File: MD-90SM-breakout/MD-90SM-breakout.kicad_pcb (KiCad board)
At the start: 2 copper layers, 21 x 14.6 mm, 13 parts, among them CON1 MD-90SM

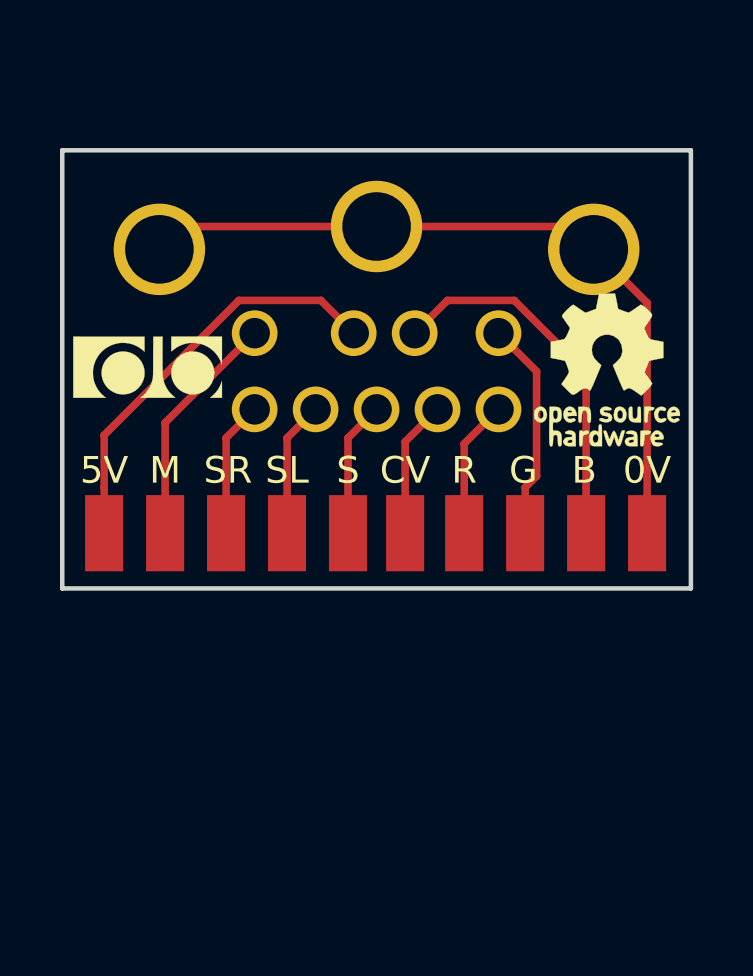
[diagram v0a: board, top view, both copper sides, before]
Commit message: updated to v0.2 with breadboard compatible dip spacing
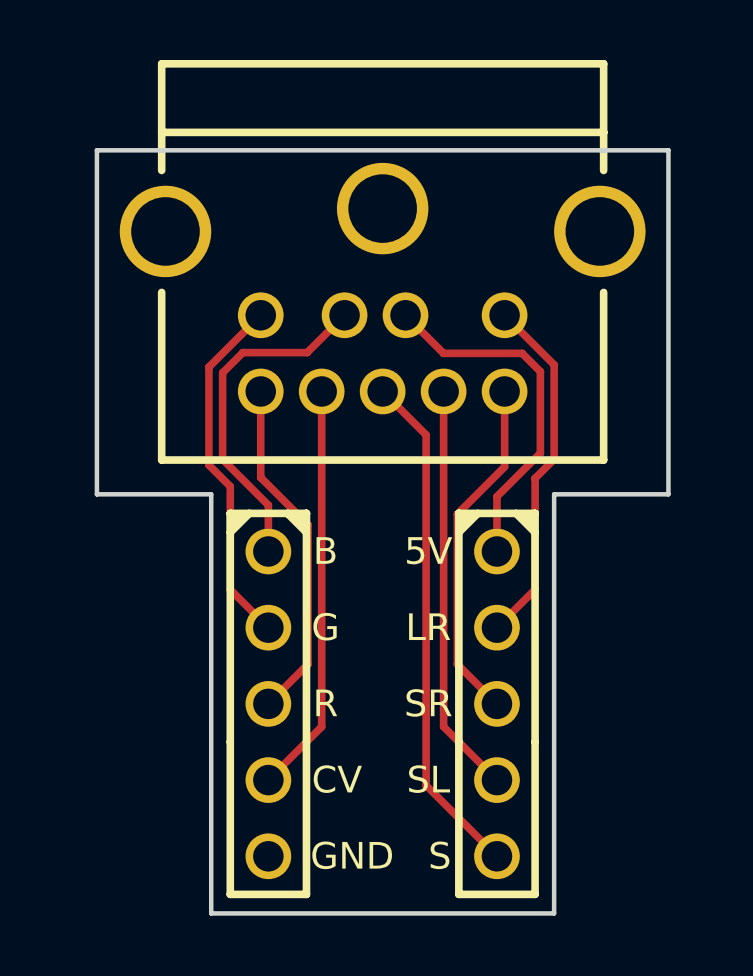
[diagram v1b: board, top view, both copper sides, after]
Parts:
- removed CON1: MD-90SM, db-thparts:MD-90SM
- removed G***: LOGO, db-artwork:db-logo_5mm
- removed G***: LOGO, db-artwork:oshw-logo_5mm
- removed TP1, TP10, TP2, TP3, TP4, TP5, TP6, TP7, TP8, TP9: TP_50x100, db-smt:TP_50-100
- added CON101: MD-90SM, db-thparts:MD-90SM, F.Cu at (149.7, 95.7)
- added CON102: PH1-05-UA, db-thparts:HDR1X5, F.Cu at (145.9, 101.0)
- added CON103: PH1-05-UA, db-thparts:HDR1X5, F.Cu at (153.6, 101.0)
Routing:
- net /GND: track 25.3 -> 0.00 mm
- net (no net): track 18.8 -> 0.00 mm
- net /S: track 4.52 -> 17.1 mm
- net /SL: track 4.52 -> 13.7 mm
- net /CV: track 4.57 -> 13.7 mm
- net /SR: track 4.52 -> 11.6 mm
- net /R: track 4.60 -> 11.6 mm
- net /G: track 7.35 -> 12.0 mm
- net /L+R: track 7.90 -> 11.9 mm
- net /+5V: track 13.9 -> 11.9 mm
- net /B: track 12.5 -> 11.4 mm
- added copper zone on B.Cu, net /GND
- added copper zone on F.Cu, net /GND
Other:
- board size 21 x 14.6 mm -> 19.1 x 25.4 mm
- net class Default removed
- rule pad_to_mask_clearance: 0.2 -> 0.1016
- board text added: "GND"
- board text added: "LR"
- board text removed: "0V"
- board text removed: "M"
